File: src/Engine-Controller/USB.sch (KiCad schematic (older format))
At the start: 1 part, among them P2 USB

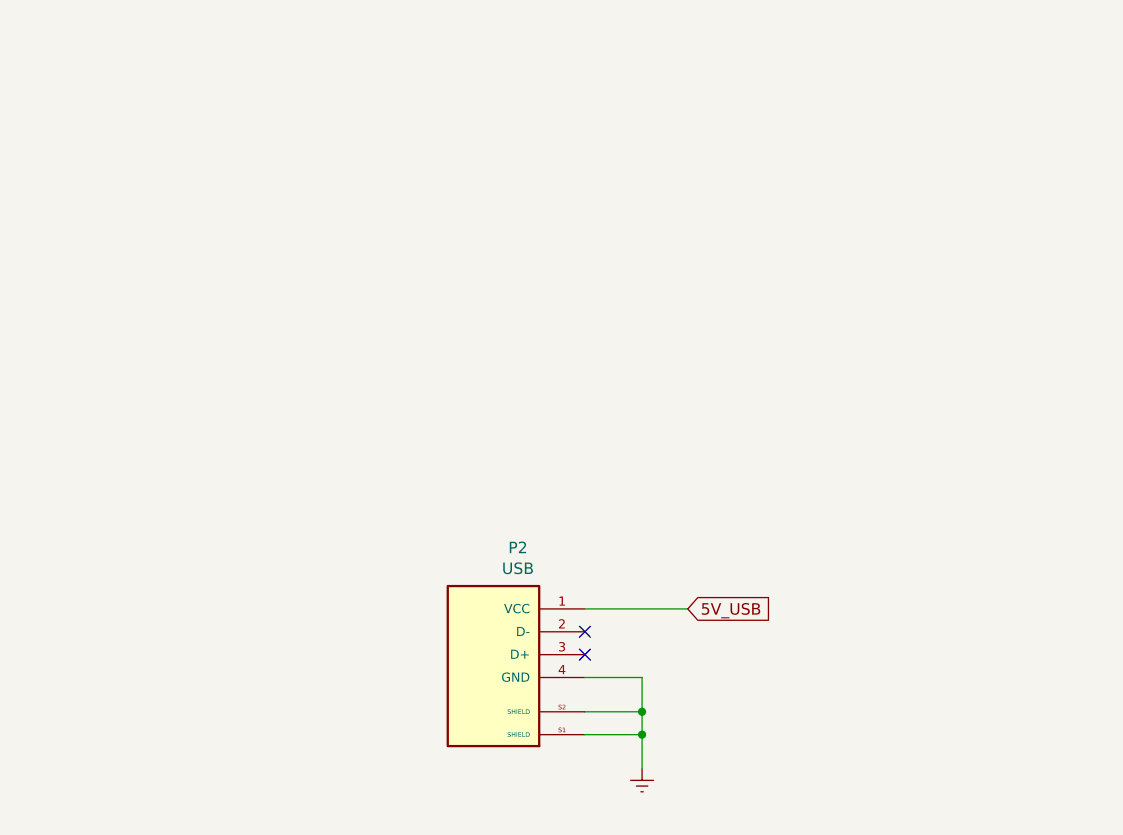
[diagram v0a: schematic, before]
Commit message: Added Ignition System to lib and schematic
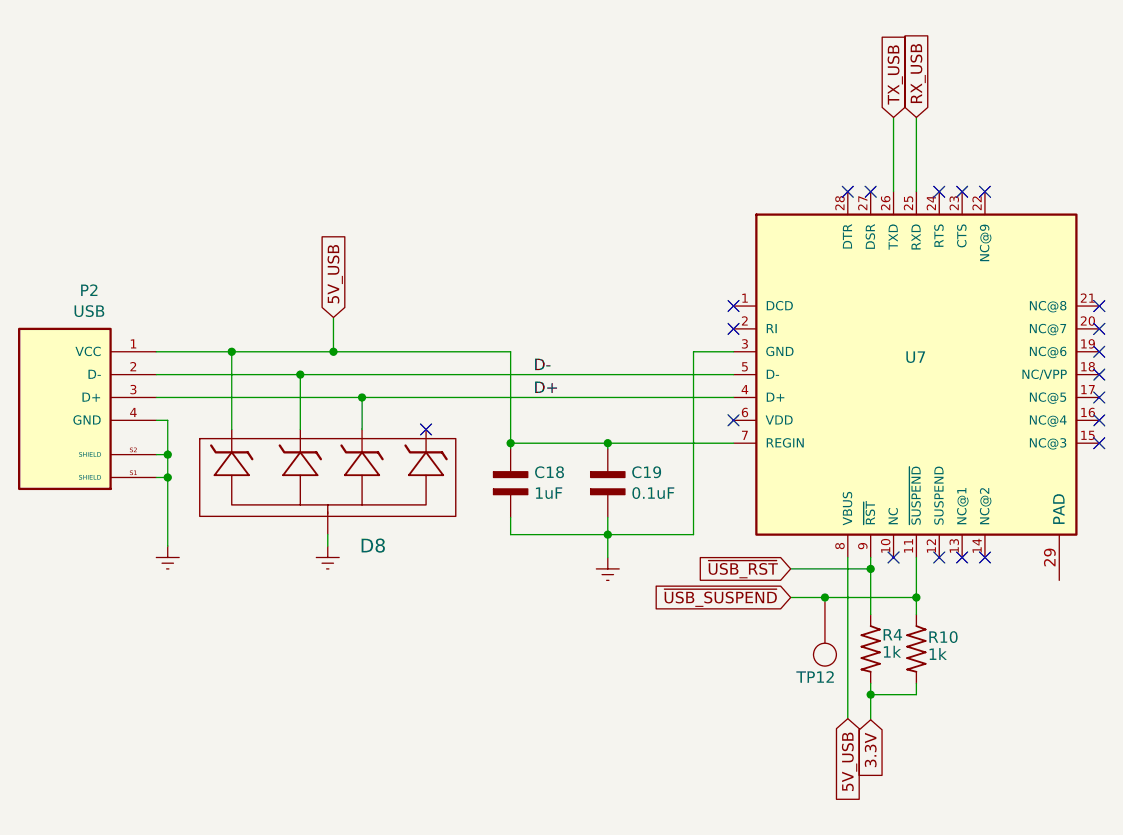
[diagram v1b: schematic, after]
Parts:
- added C18: 1uF, Engine-Controller:CAP_0603, symbol Engine-Controller:CAP_0603
- added C19: 0.1uF, Engine-Controller:CAP_0603, symbol Engine-Controller:CAP_0603
- added D8: SP0504BAHTG, Engine-Controller:SP0504BAHTG, symbol Engine-Controller:SP0504BAHTG
- added R10, R4: 1k, Engine-Controller:RES_0603, symbol Engine-Controller:RES_0603
- added TP12: TP, Engine-Controller:TP, symbol Engine-Controller:TP
- added U7: CP2102-GMR(QFN28), Engine-Controller:CP2012-GMR, symbol Engine-Controller:CP2102-GMR(QFN28)
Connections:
- net 5V_USB: now also C18.2, C19.2, D8.1, U7.7 (REGIN), U7.8 (VBUS)
- net Earth: now also C18.1, C19.1, D8.2, U7.3 (GND)
- net D-: now reaches P2.2 (D-)
- net D-: now also D8.3, U7.5 (D-)
- net D+: now reaches P2.3 (D+)
- net D+: now also D8.4, U7.4 (D+)
- new net 3.3V: R10.2, R4.2
- new net RX_USB: U7.25 (RXD)
- new net TX_USB: U7.26 (TXD)
- new net ~USB_RST: R4.1, U7.9 (~RST)
- new net ~USB_SUSPEND: R10.1, TP12.1, U7.11 (~SUSPEND)
- no-connect marks 2 -> 20
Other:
- moved on the sheet: P2

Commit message: finished routing rev3.0
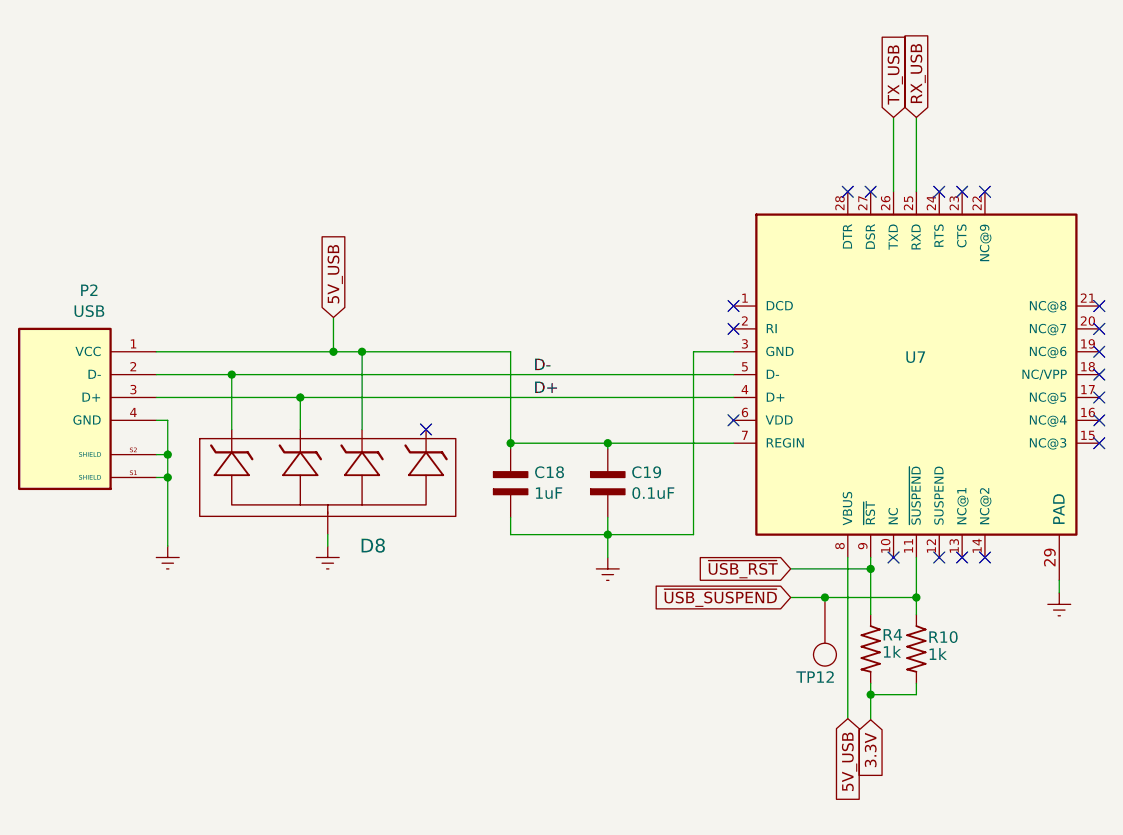
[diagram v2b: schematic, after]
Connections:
- net 5V_USB: now also D8.4; no longer D8.1
- net D+: now also D8.3; no longer D8.4
- net D-: now also D8.1; no longer D8.3
- net Earth: now also U7.29 (PAD)
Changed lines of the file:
@@
 Wire Wire Line
 	7150 2075 7150 1750
-$Comp
-L Engine-Controller:SP0504BAHTG D8
-U 1 1 617B8701
-P 4575 3365
-F 0 "D8" H 4715 3105 60  0000 L CNN
-F 1 "SP0504BAHTG" H 3825 2805 60  0001 C CNN
-F 2 "Engine-Controller:SP0504BAHTG" H 3755 2565 60  0001 C CNN
-F 3 "" V 4365 3415 60  0001 C CNN
-	1    4575 3365
-	1    0    0    -1
-$EndComp
-Wire Wire Line
-	4600 2775 5375 2775
 Wire Wire Line
 	5375 2775 5375 3175
@@
 Wire Wire Line
 	3875 3325 3875 3625
-Wire Wire Line
-	3825 2775 4155 2775
 Connection ~ 4600 2775
-Wire Wire Line
-	3825 2875 4455 2875
 $Comp
 L Engine-Controller:Earth #PWR015
@@
 	1    0    0    -1
 $EndComp
-Wire Wire Line
-	4725 3115 4725 2975
-Wire Wire Line
-	3825 2975 4725 2975
-Connection ~ 4725 2975
-Wire Wire Line
-	4725 2975 6350 2975
-Wire Wire Line
-	4455 3115 4455 2875
-Connection ~ 4455 2875
-Wire Wire Line
-	4455 2875 6350 2875
-Wire Wire Line
-	4155 3115 4155 2775
-Connection ~ 4155 2775
-Wire Wire Line
-	4155 2775 4600 2775
 NoConn ~ 5005 3115
 Wire Wire Line
@@
 Wire Wire Line
 	7150 4275 7150 4225
+Wire Wire Line
+	3825 2775 4600 2775
+Wire Wire Line
+	3825 2875 4155 2875
+Wire Wire Line
+	3825 2975 4455 2975
+$Comp
+L Engine-Controller:SP0504BAHTG D8
+U 1 1 617B8701
+P 4575 3365
+F 0 "D8" H 4715 3105 60  0000 L CNN
+F 1 "SP0504BAHTG" H 3825 2805 60  0001 C CNN
+F 2 "Engine-Controller:SP0504BAHTG" H 3755 2565 60  0001 C CNN
+F 3 "" V 4365 3415 60  0001 C CNN
+	1    4575 3365
+	1    0    0    -1
+$EndComp
+Wire Wire Line
+	4725 3115 4725 2775
+Wire Wire Line
+	4600 2775 4725 2775
+Connection ~ 4725 2775
+Wire Wire Line
+	4725 2775 5375 2775
+Wire Wire Line
+	4155 3115 4155 2875
+Connection ~ 4155 2875
+Wire Wire Line
+	4155 2875 6350 2875
+Wire Wire Line
+	4455 3115 4455 2975
+Connection ~ 4455 2975
+Wire Wire Line
+	4455 2975 6350 2975
+$Comp
+L Engine-Controller:Earth #PWR0122
+U 1 1 61B32FFB
+P 7775 3830
+F 0 "#PWR0122" H 7775 3580 50  0001 C CNN
+F 1 "Earth" H 7775 3680 50  0001 C CNN
+F 2 "" H 7775 3830 50  0001 C CNN
+F 3 "" H 7775 3830 50  0001 C CNN
+	1    7775 3830
+	1    0    0    -1
+$EndComp
+Wire Wire Line
+	7775 3775 7775 3830
 $EndSCHEMATC
